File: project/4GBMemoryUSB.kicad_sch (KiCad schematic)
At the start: 12 parts, among them J1 USB_A, J2 Conn_01x06_Socket, U1 LD1117S33TR_SOT223

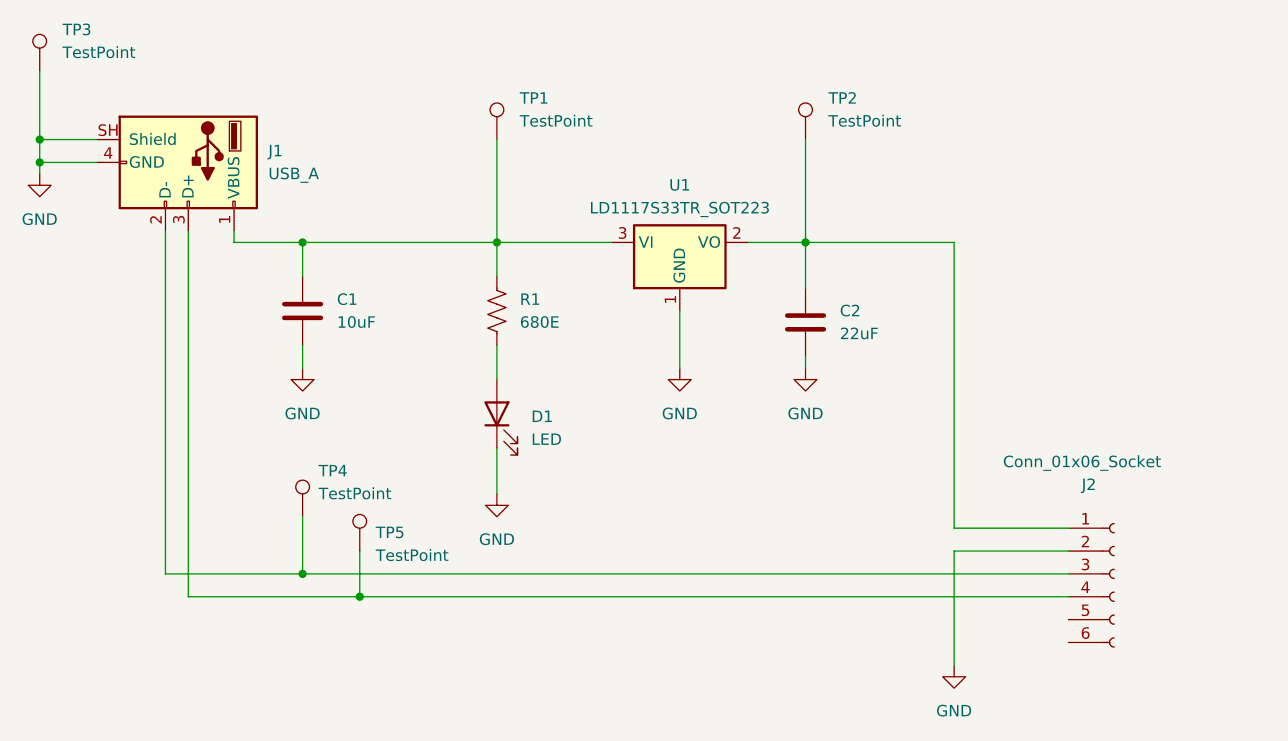
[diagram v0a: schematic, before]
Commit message: Update with photos + fix LED VCC
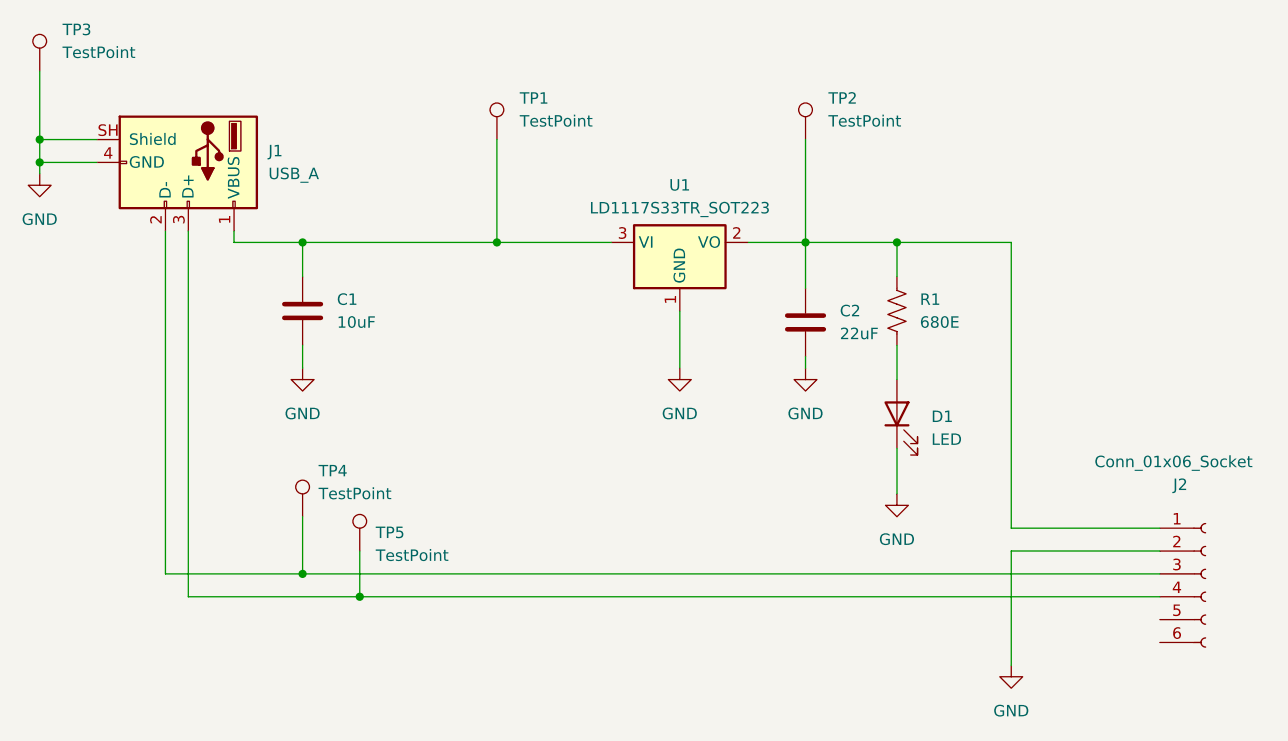
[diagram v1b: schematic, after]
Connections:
- net at C2.1, J2.1 (Pin_1), TP2.1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: now also R1.1
- net at C1.1, J1.1 (VBUS), TP1.1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: no longer R1.1
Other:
- moved on the sheet: D1, J2, R1
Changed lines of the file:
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@@
 	(paper "A4")
+	(junction
+		(at 113.03 81.28)
+		(diameter 0)
+		(color 0 0 0 0)
+	)
+	(junction
+		(at 179.07 44.45)
+		(diameter 0)
+		(color 0 0 0 0)
+	)
+	(junction
+		(at 113.03 44.45)
+		(diameter 0)
+		(color 0 0 0 0)
+	)
+	(junction
+		(at 168.91 44.45)
+		(diameter 0)
+		(color 0 0 0 0)
+	)
+	(junction
+		(at 134.62 44.45)
+		(diameter 0)
+		(color 0 0 0 0)
+	)
+	(junction
+		(at 83.82 33.02)
+		(diameter 0)
+		(color 0 0 0 0)
+	)
 	(junction
 		(at 119.38 83.82)
@@
 	)
 	(junction
-		(at 113.03 44.45)
-		(diameter 0)
-		(color 0 0 0 0)
-	)
-	(junction
-		(at 168.91 44.45)
-		(diameter 0)
-		(color 0 0 0 0)
-	)
-	(junction
-		(at 134.62 44.45)
-		(diameter 0)
-		(color 0 0 0 0)
-	)
-	(junction
-		(at 83.82 33.02)
-		(diameter 0)
-		(color 0 0 0 0)
-	)
-	(junction
-		(at 113.03 81.28)
-		(diameter 0)
-		(color 0 0 0 0)
-	)
-	(junction
 		(at 83.82 35.56)
 		(diameter 0)
@@
 	(wire
 		(pts
+			(xy 179.07 44.45) (xy 179.07 48.26)
+		)
+		(stroke
+			(width 0)
+			(type default)
+		)
+	)
+	(wire
+		(pts
 			(xy 168.91 33.02) (xy 168.91 44.45)
 		)
@@
 	(wire
 		(pts
-			(xy 198.12 78.74) (xy 185.42 78.74)
-		)
-		(stroke
-			(width 0)
-			(type default)
-		)
-	)
-	(wire
-		(pts
-			(xy 134.62 67.31) (xy 134.62 72.39)
-		)
-		(stroke
-			(width 0)
-			(type default)
-		)
-	)
-	(wire
-		(pts
-			(xy 134.62 44.45) (xy 134.62 48.26)
-		)
-		(stroke
-			(width 0)
-			(type default)
-		)
-	)
-	(wire
-		(pts
-			(xy 134.62 55.88) (xy 134.62 59.69)
+			(xy 208.28 78.74) (xy 191.77 78.74)
+		)
+		(stroke
+			(width 0)
+			(type default)
+		)
+	)
+	(wire
+		(pts
+			(xy 179.07 67.31) (xy 179.07 72.39)
+		)
+		(stroke
+			(width 0)
+			(type default)
+		)
+	)
+	(wire
+		(pts
+			(xy 179.07 55.88) (xy 179.07 59.69)
+		)
+		(stroke
+			(width 0)
+			(type default)
+		)
+	)
+	(wire
+		(pts
+			(xy 179.07 44.45) (xy 168.91 44.45)
 		)
 		(stroke
@@
 	(wire
 		(pts
-			(xy 185.42 76.2) (xy 185.42 44.45)
+			(xy 191.77 76.2) (xy 191.77 44.45)
 		)
 		(stroke
@@
 	(wire
 		(pts
-			(xy 185.42 78.74) (xy 185.42 91.44)
+			(xy 191.77 78.74) (xy 191.77 91.44)
 		)
 		(stroke
@@
 	(wire
 		(pts
-			(xy 198.12 83.82) (xy 119.38 83.82)
+			(xy 208.28 83.82) (xy 119.38 83.82)
 		)
 		(stroke
@@
 	(wire
 		(pts
-			(xy 113.03 81.28) (xy 198.12 81.28)
+			(xy 113.03 81.28) (xy 208.28 81.28)
 		)
 		(stroke
@@
 	(wire
 		(pts
-			(xy 198.12 76.2) (xy 185.42 76.2)
+			(xy 208.28 76.2) (xy 191.77 76.2)
 		)
 		(stroke
@@
 	(wire
 		(pts
-			(xy 185.42 44.45) (xy 168.91 44.45)
+			(xy 191.77 44.45) (xy 179.07 44.45)
 		)
 		(stroke
@@
 	(symbol
 		(lib_id "Device:LED")
-		(at 134.62 63.5 90)
+		(at 179.07 63.5 90)
 		(unit 1)
 		(body_style 1)
@@
 		(fields_autoplaced yes)
 		(property "Reference" "D1"
-			(at 138.43 63.8174 90)
+			(at 182.88 63.8174 90)
 			(show_name no)
 			(do_not_autoplace no)
@@
 		)
 		(property "Value" "LED"
-			(at 138.43 66.3574 90)
+			(at 182.88 66.3574 90)
 			(show_name no)
 			(do_not_autoplace no)
@@
 		)
 		(property "Footprint" "LED_SMD:LED_0603_1608Metric_Pad1.05x0.95mm_HandSolder"
-			(at 134.62 63.5 0)
+			(at 179.07 63.5 0)
 			(hide yes)
 			(show_name no)
@@
 		)
 		(property "Datasheet" ""
-			(at 134.62 63.5 0)
+			(at 179.07 63.5 0)
 			(hide yes)
 			(show_name no)
@@
 		)
 		(property "Description" "Light emitting diode"
-			(at 134.62 63.5 0)
+			(at 179.07 63.5 0)
 			(hide yes)
 			(show_name no)
@@
 		)
 		(property "Sim.Pins" "1=K 2=A"
-			(at 134.62 63.5 0)
+			(at 179.07 63.5 0)
 			(hide yes)
 			(show_name no)
@@
 	(symbol
 		(lib_id "power:GND")
-		(at 134.62 72.39 0)
+		(at 179.07 72.39 0)
 		(unit 1)
 		(body_style 1)
@@
 		(fields_autoplaced yes)
 		(property "Reference" "#PWR05"
-			(at 134.62 78.74 0)
+			(at 179.07 78.74 0)
 			(hide yes)
 			(show_name no)
@@
 		)
 		(property "Value" "GND"
-			(at 134.62 77.47 0)
+			(at 179.07 77.47 0)
 			(show_name no)
 			(do_not_autoplace no)
@@
 		)
 		(property "Footprint" ""
-			(at 134.62 72.39 0)
+			(at 179.07 72.39 0)
 			(hide yes)
 			(show_name no)
@@
 		)
 		(property "Datasheet" ""
-			(at 134.62 72.39 0)
+			(at 179.07 72.39 0)
 			(hide yes)
 			(show_name no)
@@
 		)
 		(property "Description" "Power symbol creates a global label with name \"GND\" , ground"
-			(at 134.62 72.39 0)
+			(at 179.07 72.39 0)
 			(hide yes)
 			(show_name no)
@@
 	(symbol
 		(lib_id "Connector:Conn_01x06_Socket")
-		(at 203.2 81.28 0)
+		(at 213.36 81.28 0)
 		(unit 1)
 		(body_style 1)
@@
 		(dnp no)
 		(property "Reference" "J2"
-			(at 200.406 71.374 0)
+			(at 210.566 71.374 0)
 			(show_name no)
 			(do_not_autoplace no)
@@
 		)
 		(property "Value" "Conn_01x06_Socket"
-			(at 199.644 68.834 0)
+			(at 209.804 68.834 0)
 			(show_name no)
 			(do_not_autoplace no)
@@
 		)
 		(property "Footprint" "360Footprints:MemoryUnitConnector"
-			(at 203.2 81.28 0)
+			(at 213.36 81.28 0)
 			(hide yes)
 			(show_name no)
@@
 		)
 		(property "Datasheet" ""
-			(at 203.2 81.28 0)
+			(at 213.36 81.28 0)
 			(hide yes)
 			(show_name no)
@@
 		)
 		(property "Description" "Generic connector, single row, 01x06, script generated"
-			(at 203.2 81.28 0)
+			(at 213.36 81.28 0)
 			(hide yes)
 			(show_name no)
@@
 	(symbol
 		(lib_id "power:GND")
-		(at 185.42 91.44 0)
+		(at 191.77 91.44 0)
 		(unit 1)
 		(body_style 1)
@@
 		(fields_autoplaced yes)
 		(property "Reference" "#PWR02"
-			(at 185.42 97.79 0)
+			(at 191.77 97.79 0)
 			(hide yes)
 			(show_name no)
@@
 		)
 		(property "Value" "GND"
-			(at 185.42 96.52 0)
+			(at 191.77 96.52 0)
 			(show_name no)
 			(do_not_autoplace no)
@@
 		)
 		(property "Footprint" ""
-			(at 185.42 91.44 0)
+			(at 191.77 91.44 0)
 			(hide yes)
 			(show_name no)
@@
 		)
 		(property "Datasheet" ""
-			(at 185.42 91.44 0)
+			(at 191.77 91.44 0)
 			(hide yes)
 			(show_name no)
@@
 		)
 		(property "Description" "Power symbol creates a global label with name \"GND\" , ground"
-			(at 185.42 91.44 0)
+			(at 191.77 91.44 0)
 			(hide yes)
 			(show_name no)
@@
 	(symbol
 		(lib_id "Device:R_US")
-		(at 134.62 52.07 0)
+		(at 179.07 52.07 0)
 		(unit 1)
 		(body_style 1)
@@
 		(fields_autoplaced yes)
 		(property "Reference" "R1"
-			(at 137.16 50.7999 0)
+			(at 181.61 50.7999 0)
 			(show_name no)
 			(do_not_autoplace no)
@@
 		)
 		(property "Value" "680E"
-			(at 137.16 53.3399 0)
+			(at 181.61 53.3399 0)
 			(show_name no)
 			(do_not_autoplace no)
@@
 		)
 		(property "Footprint" "Resistor_SMD:R_0603_1608Metric_Pad0.98x0.95mm_HandSolder"
-			(at 135.636 52.324 90)
+			(at 180.086 52.324 90)
 			(hide yes)
 			(show_name no)
@@
 		)
 		(property "Datasheet" ""
-			(at 134.62 52.07 0)
+			(at 179.07 52.07 0)
 			(hide yes)
 			(show_name no)
@@
 		)
 		(property "Description" "Resistor, US symbol"
-			(at 134.62 52.07 0)
-			(hide yes)
-			(show_name no)
+			(at 179.07 52.07 0)
+			(hide yes)
+			(show_name no)
